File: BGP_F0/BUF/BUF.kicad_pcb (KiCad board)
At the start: 2 copper layers, 41 x 26 mm, 36 parts, among them P1 CONN_01X02, P2 CONN_01X02, P3 CONN_01X03, P4 CONN_01X02, P5 CONN_01X02, P6 CONN_01X09, P7 CONN_01X03, P8 CONN_01X05, Q1 2SK208, Q2 2SK208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

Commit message: F0 prot diode added, bt changed to 26mm
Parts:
- added D1: CS1D, Diodes_SMD:D_SMA, B.Cu at (134.8, 99.0)
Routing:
- net Earth: track 99.7 -> 104.4 mm, vias 2 -> 3
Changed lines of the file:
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@@
-(kicad_pcb (version 4) (host pcbnew 4.0.4-1.fc24-product)
+(kicad_pcb (version 4) (host pcbnew 4.0.7)
   (general
-    (links 71)
+    (links 73)
     (no_connects 0)
-    (area 120.15412 74.499999 163.225001 104.375001)
+    (area 121.924999 77.924999 163.075001 104.075001)
     (thickness 1.2)
     (drawings 8)
-    (tracks 224)
+    (tracks 231)
     (zones 0)
-    (modules 36)
+    (modules 37)
     (nets 24)
   )
@@
     (0 F.Cu signal)
     (31 B.Cu signal)
-    (32 B.Adhes user hide)
-    (33 F.Adhes user hide)
-    (34 B.Paste user hide)
-    (35 F.Paste user hide)
-    (36 B.SilkS user hide)
-    (37 F.SilkS user hide)
-    (38 B.Mask user hide)
-    (39 F.Mask user hide)
-    (40 Dwgs.User user hide)
-    (41 Cmts.User user hide)
-    (42 Eco1.User user hide)
-    (43 Eco2.User user hide)
-    (44 Edge.Cuts user hide)
-    (45 Margin user hide)
-    (46 B.CrtYd user hide)
-    (47 F.CrtYd user hide)
-    (48 B.Fab user hide)
-    (49 F.Fab user hide)
+    (32 B.Adhes user)
+    (33 F.Adhes user)
+    (34 B.Paste user)
+    (35 F.Paste user)
+    (36 B.SilkS user)
+    (37 F.SilkS user)
+    (38 B.Mask user)
+    (39 F.Mask user)
+    (40 Dwgs.User user)
+    (41 Cmts.User user)
+    (42 Eco1.User user)
+    (43 Eco2.User user)
+    (44 Edge.Cuts user)
+    (45 Margin user)
+    (46 B.CrtYd user)
+    (47 F.CrtYd user)
+    (48 B.Fab user)
+    (49 F.Fab user)
   )
   (setup
@@
       (net 8 Earth))
     (model ${KISYS3DMOD}/TO_SOT_Packages_SMD.3dshapes/SC-59.wrl
+      (at (xyz 0 0 0))
+      (scale (xyz 1 1 1))
+      (rotate (xyz 0 0 0))
+    )
+  )
+  (module Diodes_SMD:D_SMA (layer B.Cu)
+    (at 134.8 99)
+    (descr "Diode SMA (DO-214AC)")
+    (tags "Diode SMA (DO-214AC)")
+    (attr smd)
+    (fp_text reference D1 (at -3 2.175001) (layer B.SilkS)
+      (effects (font (size 0.6 0.6) (thickness 0.15)) (justify mirror))
+    )
+    (fp_text value CS1D (at 0 -2.6) (layer B.Fab) hide
+      (effects (font (size 0.6 0.6) (thickness 0.15)) (justify mirror))
+    )
+    (fp_text user %R (at 0 2.5) (layer B.Fab) hide
+      (effects (font (size 1 1) (thickness 0.15)) (justify mirror))
+    )
+    (fp_line (start -3.4 1.65) (end -3.4 -1.65) (layer B.SilkS) (width 0.12))
+    (fp_line (start 2.3 -1.5) (end -2.3 -1.5) (layer B.Fab) (width 0.1))
+    (fp_line (start -2.3 -1.5) (end -2.3 1.5) (layer B.Fab) (width 0.1))
+    (fp_line (start 2.3 1.5) (end 2.3 -1.5) (layer B.Fab) (width 0.1))
+    (fp_line (start 2.3 1.5) (end -2.3 1.5) (layer B.Fab) (width 0.1))
+    (fp_line (start -3.5 1.75) (end 3.5 1.75) (layer B.CrtYd) (width 0.05))
+    (fp_line (start 3.5 1.75) (end 3.5 -1.75) (layer B.CrtYd) (width 0.05))
+    (fp_line (start 3.5 -1.75) (end -3.5 -1.75) (layer B.CrtYd) (width 0.05))
+    (fp_line (start -3.5 -1.75) (end -3.5 1.75) (layer B.CrtYd) (width 0.05))
+    (fp_line (start -0.64944 -0.00102) (end -1.55114 -0.00102) (layer B.Fab) (width 0.1))
+    (fp_line (start 0.50118 -0.00102) (end 1.4994 -0.00102) (layer B.Fab) (width 0.1))
+    (fp_line (start -0.64944 0.79908) (end -0.64944 -0.80112) (layer B.Fab) (width 0.1))
+    (fp_line (start 0.50118 -0.75032) (end 0.50118 0.79908) (layer B.Fab) (width 0.1))
+    (fp_line (start -0.64944 -0.00102) (end 0.50118 -0.75032) (layer B.Fab) (width 0.1))
+    (fp_line (start -0.64944 -0.00102) (end 0.50118 0.79908) (layer B.Fab) (width 0.1))
+    (fp_line (start -3.4 -1.65) (end 2 -1.65) (layer B.SilkS) (width 0.12))
+    (fp_line (start -3.4 1.65) (end 2 1.65) (layer B.SilkS) (width 0.12))
+    (pad 1 smd rect (at -2 0) (size 2.5 1.8) (layers B.Cu B.Paste B.Mask)
+      (net 20 /V+))
+    (pad 2 smd rect (at 2 0) (size 2.5 1.8) (layers B.Cu B.Paste B.Mask)
+      (net 8 Earth))
+    (model ${KISYS3DMOD}/Diodes_SMD.3dshapes/D_SMA.wrl
       (at (xyz 0 0 0))
       (scale (xyz 1 1 1))
@@
   (segment (start 139 97.05) (end 135.35 97.05) (width 0.25) (layer F.Cu) (net 7))
   (segment (start 135.35 97.05) (end 135.3 97.1) (width 0.25) (layer F.Cu) (net 7))
+  (segment (start 137 95.8) (end 137 98.8) (width 0.5) (layer B.Cu) (net 8))
+  (segment (start 137 98.8) (end 136.8 99) (width 0.5) (layer B.Cu) (net 8))
+  (segment (start 136.6 94.55) (end 136.6 95.4) (width 0.5) (layer F.Cu) (net 8))
+  (via (at 137 95.8) (size 0.6) (drill 0.4) (layers F.Cu B.Cu) (net 8))
+  (segment (start 136.6 95.4) (end 137 95.8) (width 0.5) (layer F.Cu) (net 8))
   (segment (start 126.8 92.8) (end 132.845518 92.8) (width 0.5) (layer B.Cu) (net 8))
   (via (at 132.8 92.8) (size 0.6) (drill 0.4) (layers F.Cu B.Cu) (net 8))
@@
   (segment (start 157.5 87.3) (end 157.5 86.3) (width 0.25) (layer F.Cu) (net 19))
   (segment (start 157.5 86.3) (end 156 84.8) (width 0.25) (layer F.Cu) (net 19))
+  (segment (start 132.8 99) (end 132.8 102.300001) (width 0.5) (layer B.Cu) (net 20))
+  (segment (start 132.8 102.300001) (end 132.700001 102.4) (width 0.5) (layer B.Cu) (net 20))
+  (segment (start 132.700001 102.4) (end 126.99949 102.4) (width 0.5) (layer B.Cu) (net 20))
+  (segment (start 132.8 99) (end 132.8 95.1) (width 0.5) (layer B.Cu) (net 20))
+  (segment (start 132.8 95.1) (end 133 94.9) (width 0.5) (layer B.Cu) (net 20))
   (segment (start 126.99949 102.4) (end 146.6 102.4) (width 0.5) (layer B.Cu) (net 20))
   (segment (start 146.6 102.4) (end 147 102) (width 0.5) (layer B.Cu) (net 20))
@@
   (segment (start 136.925 87.895) (end 135.574987 89.245013) (width 0.5) (layer F.Cu) (net 20))
   (segment (start 138.2 87.895) (end 136.925 87.895) (width 0.5) (layer F.Cu) (net 20))
-  (segment (start 126.99949 102.4) (end 132.700001 102.4) (width 0.5) (layer B.Cu) (net 20))
-  (segment (start 132.700001 102.4) (end 132.700001 95.199999) (width 0.5) (layer B.Cu) (net 20))
-  (segment (start 132.700001 95.199999) (end 133 94.9) (width 0.5) (layer B.Cu) (net 20))
   (segment (start 132 94.9) (end 133 94.9) (width 0.5) (layer F.Cu) (net 20))
   (via (at 133 94.9) (size 0.6) (drill 0.4) (layers F.Cu B.Cu) (net 20))

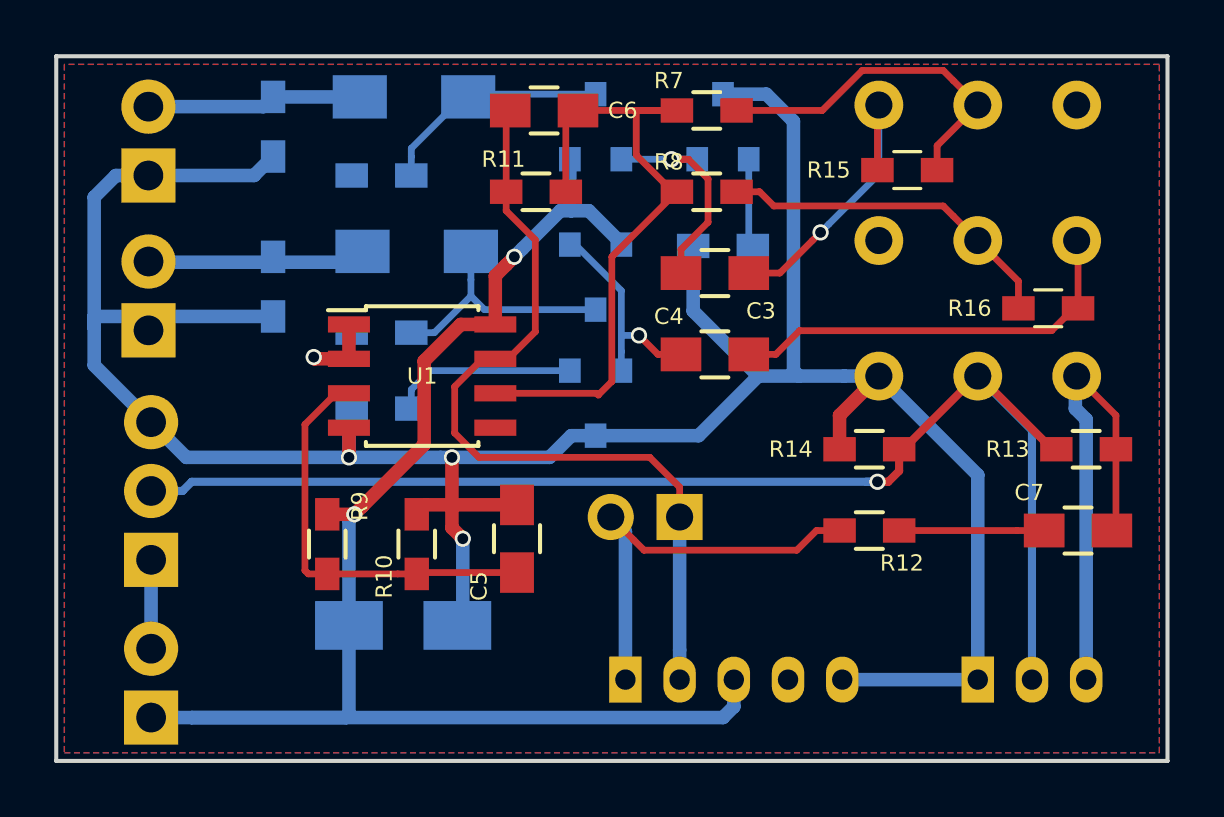
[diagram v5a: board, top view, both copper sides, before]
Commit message: Removed old boards, all F0 are now 26mm deep
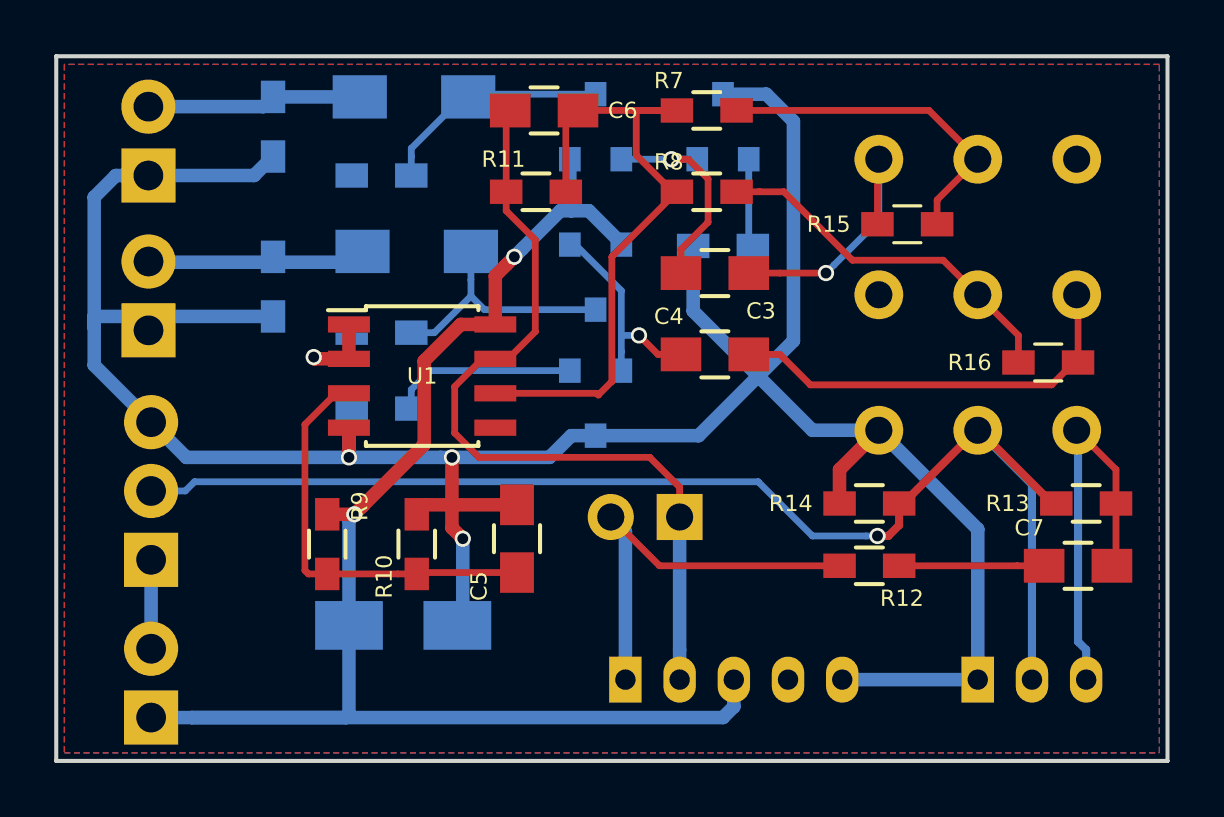
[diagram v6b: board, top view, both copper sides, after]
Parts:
- moved P6 2.00 mm to (152.3, 81.8)
- moved R13 2.00 mm to (160.0, 94.5)
- moved R14 2.00 mm to (152.0, 94.5)
- moved R15 2.00 mm to (153.4, 84.2)
- moved R16 2.00 mm to (158.6, 89.3)
- moved C7 1.30 mm to (159.7, 96.8)
- moved R12 1.30 mm to (152.0, 96.8)
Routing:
- net /PV_3: track 18.2 -> 15.4 mm
- net /PV_2: track 49.2 -> 47.6 mm
- net /PB1_1: track 11.3 -> 10.3 mm
- net /PB2_2: track 12.8 -> 13.6 mm
- net Earth: track 104.4 -> 103.7 mm

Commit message: Started work on Discrete Version
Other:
- board text added: "B+ B-"
- board text added: "BT- BT+"
- board text added: "G O -"
- board text added: "N+ N-"
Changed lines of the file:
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@@
-(kicad_pcb (version 4) (host pcbnew 4.0.4-1.fc24-product)
+(kicad_pcb (version 4) (host pcbnew 4.0.7)
   (general
     (links 73)
-    (no_connects 0)
-    (area 120.15412 74.499999 163.225001 104.375001)
+    (no_connects 2)
+    (area 121.924999 77.924999 163.075001 104.075001)
     (thickness 1.2)
-    (drawings 8)
+    (drawings 12)
     (tracks 225)
     (zones 0)
@@
     )
     (fp_text user %R (at 0 2.5) (layer B.Fab) hide
-      (effects (font (size 1 1) (thickness 0.15)) (justify mirror))
+      (effects (font (size 0.6 0.6) (thickness 0.15)) (justify mirror))
     )
     (fp_line (start -3.4 1.65) (end -3.4 -1.65) (layer B.SilkS) (width 0.12))
@@
       (rotate (xyz 0 0 0))
     )
+  )
+  (gr_text "BT-\n\n\nBT+" (at 123.3 101) (layer F.SilkS)
+    (effects (font (size 0.6 0.6) (thickness 0.15)))
+  )
+  (gr_text "G\n\nO\n\n-" (at 122.9 94) (layer F.SilkS)
+    (effects (font (size 0.6 0.6) (thickness 0.15)))
+  )
+  (gr_text "B+\n\n\nB-" (at 123.2 87) (layer F.SilkS)
+    (effects (font (size 0.6 0.6) (thickness 0.15)))
+  )
+  (gr_text "N+\n\n\nN-" (at 123.2 81) (layer F.SilkS)
+    (effects (font (size 0.6 0.6) (thickness 0.15)))
   )
   (gr_line (start 162.7 103.7) (end 162.7 78.3) (layer Margin) (width 0.2))
@@
   (segment (start 139 97.05) (end 135.35 97.05) (width 0.25) (layer F.Cu) (net 7))
   (segment (start 135.35 97.05) (end 135.3 97.1) (width 0.25) (layer F.Cu) (net 7))
-  (segment (start 149.199999 80.399999) (end 149.199999 88.500001) (width 0.5) (layer B.Cu) (net 8))
-  (segment (start 149.199999 88.500001) (end 147.9 89.8) (width 0.5) (layer B.Cu) (net 8))
-  (segment (start 152.35 91.8) (end 149.9 91.8) (width 0.5) (layer B.Cu) (net 8))
-  (segment (start 149.9 91.8) (end 147.9 89.8) (width 0.5) (layer B.Cu) (net 8))
+  (segment (start 145.5 85) (end 145.65 85) (width 0.5) (layer B.Cu) (net 8))
+  (segment (start 145.65 85) (end 149.1 88.45) (width 0.5) (layer B.Cu) (net 8))
+  (segment (start 149.1 88.45) (end 149.1 88.55) (width 0.5) (layer B.Cu) (net 8))
+  (segment (start 149.1 81) (end 149.1 88.55) (width 0.5) (layer B.Cu) (net 8))
+  (segment (start 149.1 88.55) (end 152.35 91.8) (width 0.5) (layer B.Cu) (net 8))
+  (segment (start 146.6 79.4) (end 147.5 79.4) (width 0.5) (layer B.Cu) (net 8))
+  (segment (start 147.5 79.4) (end 149.1 81) (width 0.5) (layer B.Cu) (net 8))
+  (segment (start 152.35 91.8) (end 152.15 92) (width 0.5) (layer B.Cu) (net 8))
+  (segment (start 152.15 92) (end 147.5 92) (width 0.5) (layer B.Cu) (net 8))
+  (segment (start 147.5 92) (end 141.9 92) (width 0.5) (layer B.Cu) (net 8))
   (segment (start 156 95.45) (end 156 101) (width 0.5) (layer B.Cu) (net 8))
   (segment (start 156 95.45) (end 152.35 91.8) (width 0.5) (layer B.Cu) (net 8))
@@
   (segment (start 123.4 89.4) (end 125.5 91.5) (width 0.5) (layer B.Cu) (net 8))
   (segment (start 124.2 82.4) (end 123.4 83.2) (width 0.5) (layer B.Cu) (net 8))
-  (segment (start 141.9 92) (end 145.7 92) (width 0.5) (layer B.Cu) (net 8))
-  (segment (start 145.7 92) (end 147.9 89.8) (width 0.5) (layer B.Cu) (net 8))
-  (segment (start 146.6 79.4) (end 148.2 79.4) (width 0.5) (layer B.Cu) (net 8))
-  (segment (start 148.2 79.4) (end 149.199999 80.399999) (width 0.5) (layer B.Cu) (net 8))
-  (segment (start 145.5 85) (end 145.5 87.4) (width 0.5) (layer B.Cu) (net 8))
-  (segment (start 145.5 87.4) (end 147.9 89.8) (width 0.5) (layer B.Cu) (net 8))
   (segment (start 125.4 82.4) (end 129.3 82.4) (width 0.5) (layer B.Cu) (net 8))
   (segment (start 129.3 82.4) (end 130 81.7) (width 0.5) (layer B.Cu) (net 8))

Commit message: Some Changes
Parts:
- removed Q3, Q4: 2SK208, TO_SOT_Packages_SMD:SC-59
- removed R5: 20k, Resistors_SMD:R_0603_HandSoldering
- added C8: 27p, Capacitors_SMD:C_0603_HandSoldering, F.Cu at (133.8, 79.9)
- added C9: 27p, Capacitors_SMD:C_0603_HandSoldering, F.Cu at (133.9, 85.6)
- added D2: S-301, Diodes_SMD:SOD-123, B.Cu at (146.1, 81.5)
- added D3: S-301, Diodes_SMD:SOD-123, B.Cu at (146.1, 87.0)
- Q1, Q2: value 2SK208 -> 2N5457
- R1, R2: value 499k -> 1.5MEG
- moved P6 0.10 mm to (152.2, 81.8)
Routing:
- net Earth: track 103.7 -> 111.3 mm
- net Net-(Q4-Pad1): track 6.84 -> 0.00 mm
- net Net-(Q3-Pad1): track 3.26 -> 0.00 mm
- net Net-(C2-Pad1): track 9.22 -> 12.2 mm, vias 0 -> 1
- net Net-(C4-Pad1): track 8.04 -> 10.2 mm
- net Net-(C1-Pad1): track 8.63 -> 10.1 mm, vias 0 -> 1
- net Net-(C3-Pad1): track 9.29 -> 9.96 mm
